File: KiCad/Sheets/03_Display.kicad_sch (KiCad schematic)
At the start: 1 part, among them U2 OLED_SSD1306_SPI_0.96

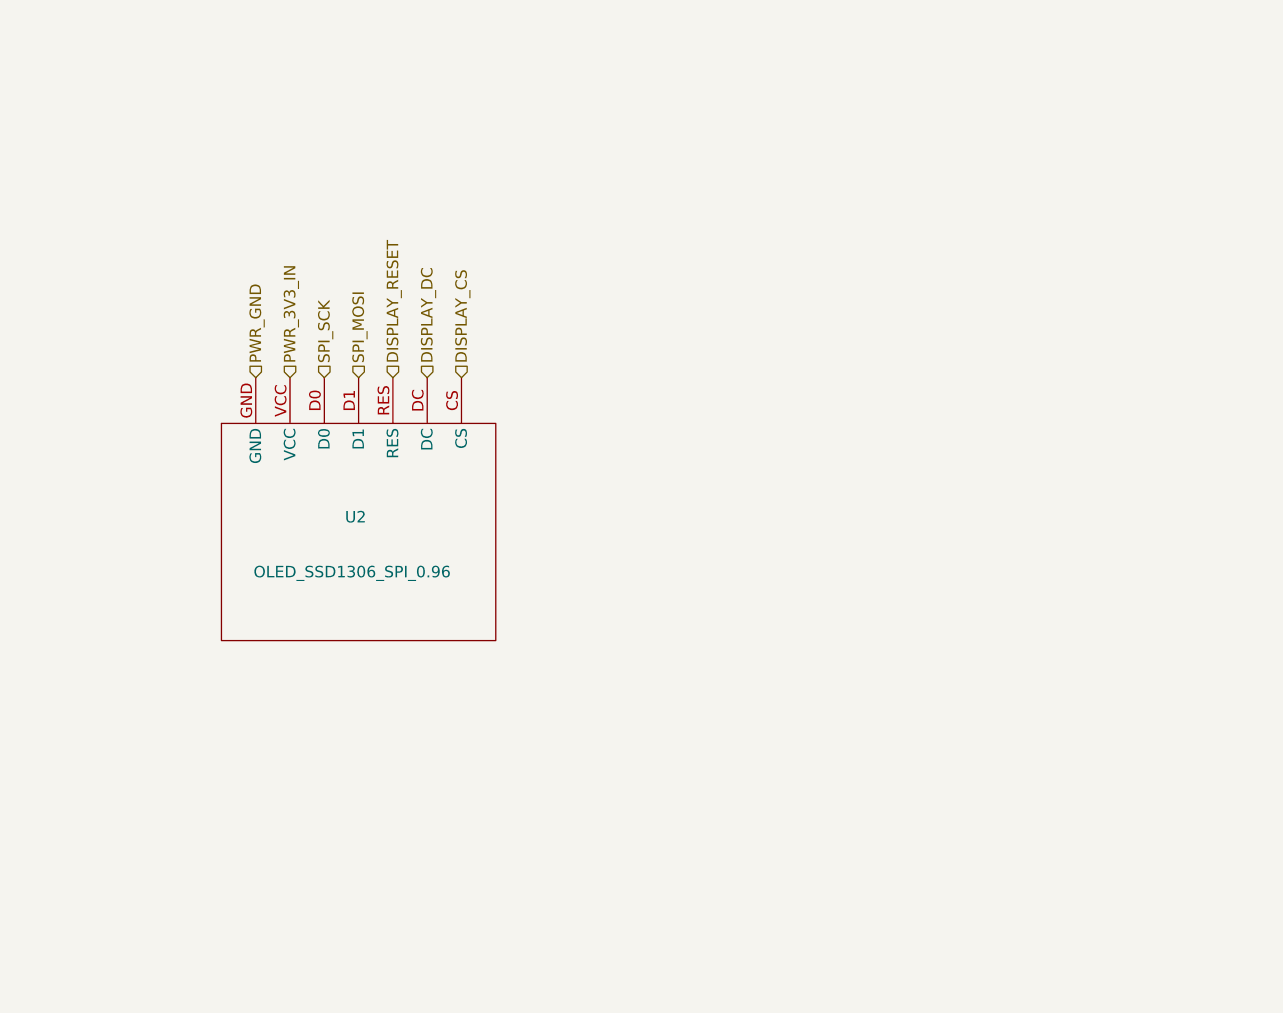
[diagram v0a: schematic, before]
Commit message: Footprints are created and assigned
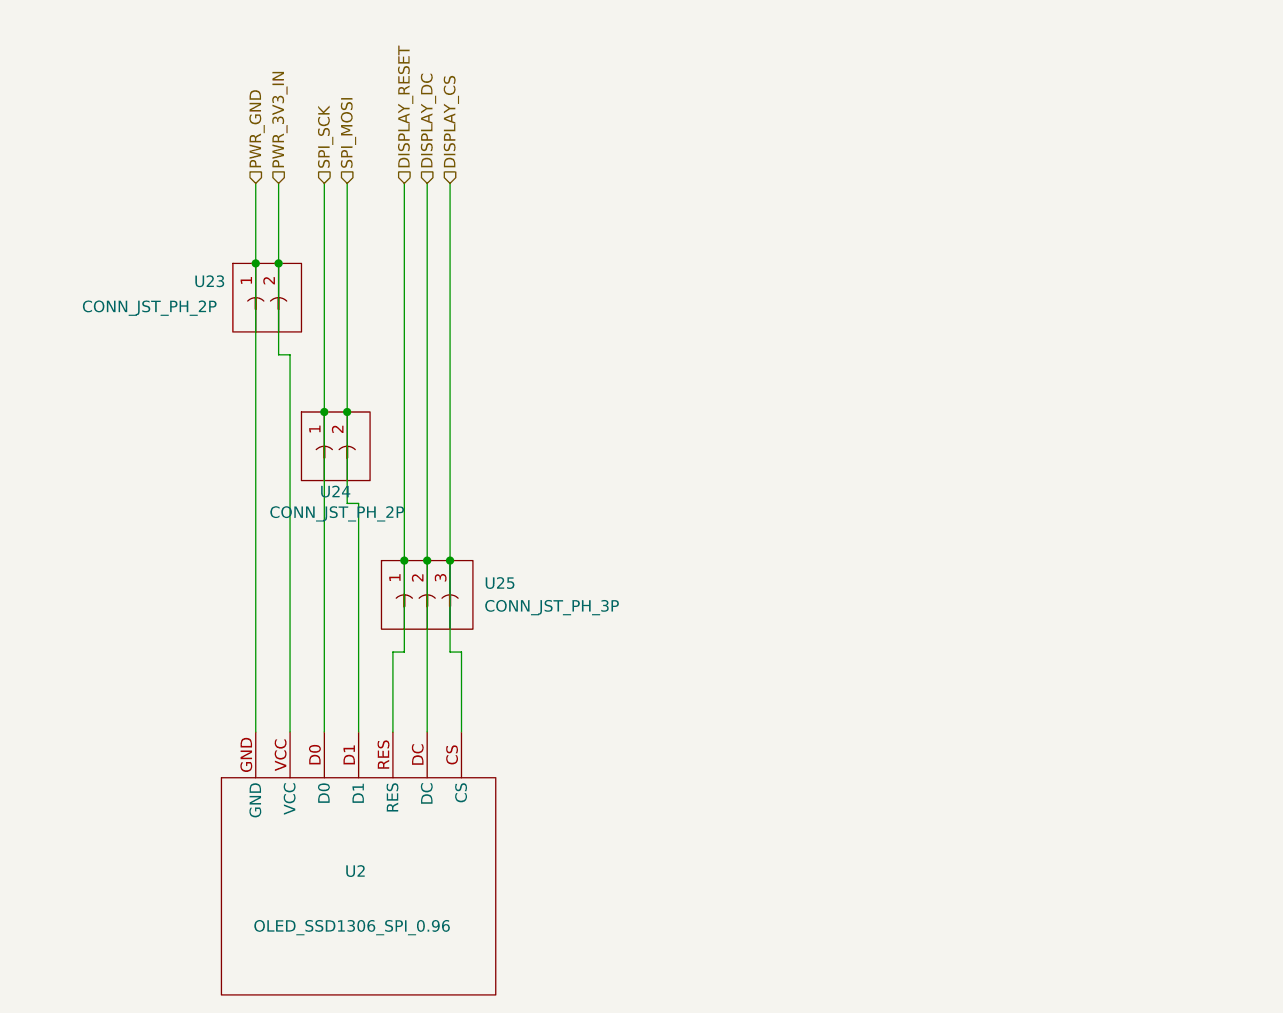
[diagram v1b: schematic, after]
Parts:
- added U23, U24: CONN_JST_PH_2P, Connector_JST:JST_PH_B2B-PH-K_1x02_P2.00mm_Vertical, symbol HMS_Symbols:CONN_JST_PH_2P
- added U25: CONN_JST_PH_3P, Connector_JST:JST_PH_B3B-PH-K_1x03_P2.00mm_Vertical, symbol HMS_Symbols:CONN_JST_PH_3P
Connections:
- net DISPLAY_CS: now also U25.3
- net DISPLAY_DC: now also U25.2
- net DISPLAY_RESET: now also U25.1
- net PWR_3V3_IN: now also U23.2
- net PWR_GND: now also U23.1
- net SPI_MOSI: now also U24.2
- net SPI_SCK: now also U24.1
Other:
- moved on the sheet: U2

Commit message: LEDs sheet added, schematic finished
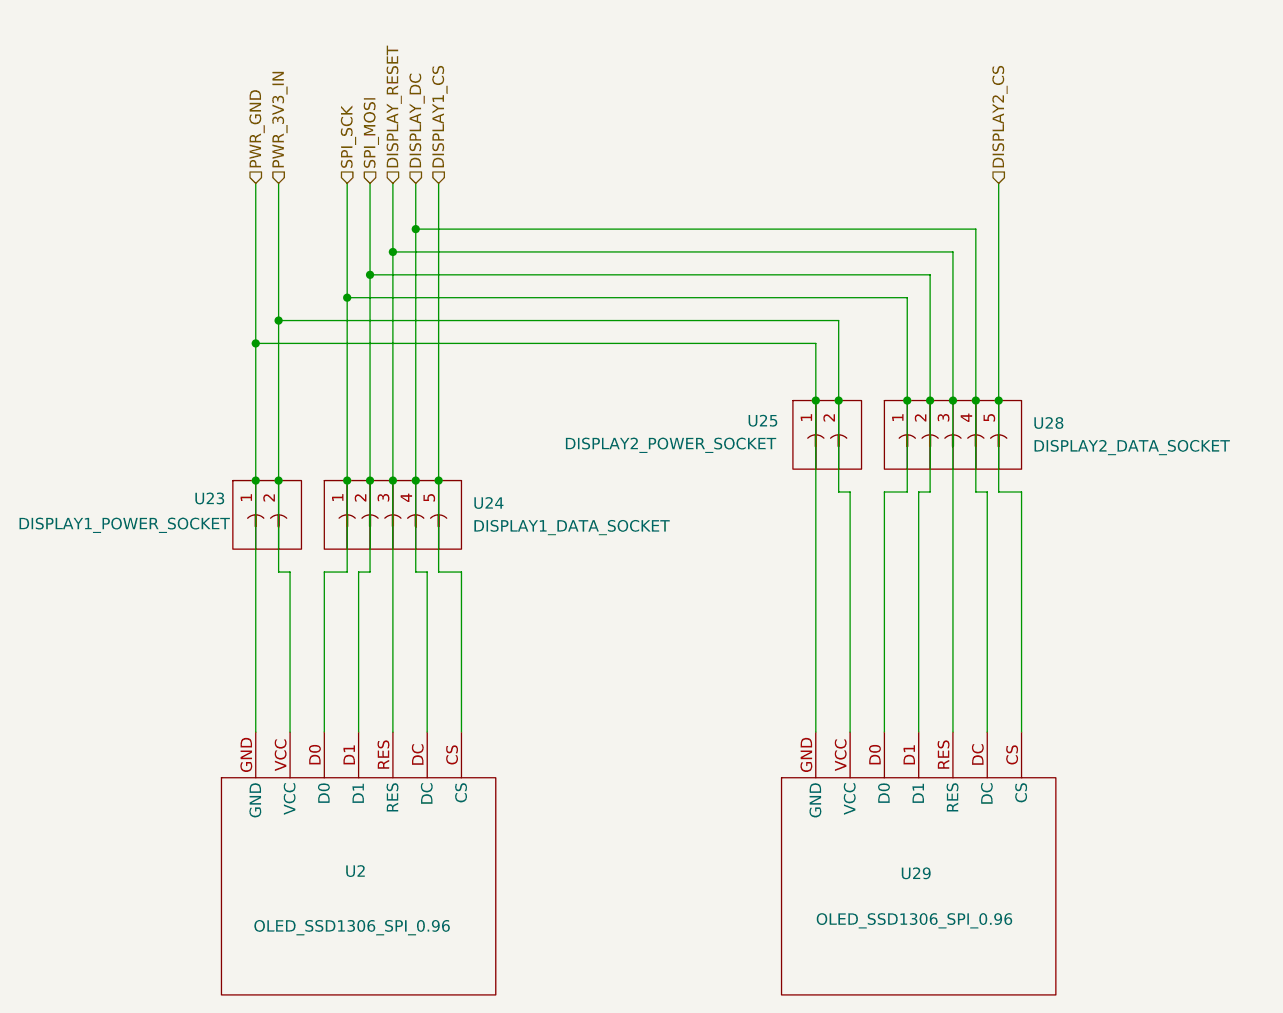
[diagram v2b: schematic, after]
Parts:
- removed U24: CONN_JST_PH_2P, Connector_JST:JST_PH_B2B-PH-K_1x02_P2.00mm_Vertical, symbol HMS_Symbols:CONN_JST_PH_2P
- removed U25: CONN_JST_PH_3P, Connector_JST:JST_PH_B3B-PH-K_1x03_P2.00mm_Vertical, symbol HMS_Symbols:CONN_JST_PH_3P
- added U24: DISPLAY1_DATA_SOCKET, Connector_JST:JST_PH_B5B-PH-K_1x05_P2.00mm_Vertical, symbol HMS_Symbols:CONN_JST_PH_5P
- added U25: DISPLAY2_POWER_SOCKET, Connector_JST:JST_PH_B2B-PH-K_1x02_P2.00mm_Vertical, symbol HMS_Symbols:CONN_JST_PH_2P
- added U28: DISPLAY2_DATA_SOCKET, Connector_JST:JST_PH_B5B-PH-K_1x05_P2.00mm_Vertical, symbol HMS_Symbols:CONN_JST_PH_5P
- added U29: OLED_SSD1306_SPI_0.96, symbol HMS_Symbols:OLED_SSD1306_SPI_0.96
- U23: value CONN_JST_PH_2P -> DISPLAY1_POWER_SOCKET
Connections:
- net DISPLAY_DC: now also U24.4, U28.4, U29.DC
- net DISPLAY_RESET: now also U24.3, U28.3, U29.RES
- net PWR_3V3_IN: now also U25.2, U29.VCC
- net PWR_GND: now also U25.1, U29.GND
- net SPI_MOSI: now also U24.2, U28.2, U29.D1
- net SPI_SCK: now also U24.1, U28.1, U29.D0
- net DISPLAY_CS renamed DISPLAY1_CS
- net DISPLAY1_CS: now also U24.5
- new net DISPLAY2_CS: U28.5, U29.CS
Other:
- moved on the sheet: U23

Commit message: Finished PCB
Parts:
- added R14, R15: 100Ω, Resistor_THT:R_Axial_DIN0207_L6.3mm_D2.5mm_P7.62mm_Horizontal, symbol Device:R
- U23, U25: footprint Connector_JST:JST_PH_B2B-PH-K_1x02_P2.00mm_Vertical -> Connector_JST:JST_XH_B2B-XH-A_1x02_P2.50mm_Vertical
- U24, U28: footprint Connector_JST:JST_PH_B5B-PH-K_1x05_P2.00mm_Vertical -> Connector_JST:JST_XH_B5B-XH-A_1x05_P2.50mm_Vertical
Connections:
- net DISPLAY1_CS: now also R14.1; no longer U2.CS, U24.5
- net DISPLAY2_CS: now also R15.1; no longer U28.5, U29.CS
- new net: R14.2, U2.CS, U24.5
- new net: R15.2, U28.5, U29.CS
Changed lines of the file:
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@@
 	(wire
 		(pts
-			(xy 214.63 63.5) (xy 214.63 87.63)
+			(xy 214.63 63.5) (xy 214.63 71.12)
 		)
 		(stroke
@@
 	(wire
 		(pts
-			(xy 152.4 63.5) (xy 152.4 96.52)
+			(xy 152.4 63.5) (xy 152.4 83.82)
 		)
 		(stroke
@@
 	(wire
 		(pts
+			(xy 152.4 91.44) (xy 152.4 96.52)
+		)
+		(stroke
+			(width 0.254)
+			(type default)
+			(color 255 153 0 1)
+		)
+	)
+	(wire
+		(pts
 			(xy 144.78 63.5) (xy 144.78 73.66)
 		)
@@
 			(type default)
 			(color 255 153 0 1)
+		)
+	)
+	(wire
+		(pts
+			(xy 214.63 78.74) (xy 214.63 87.63)
+		)
+		(stroke
+			(width 0.254)
+			(type default)
+			(color 132 132 132 1)
 		)
 	)
@@
 			)
 		)
-		(property "Footprint" "Connector_JST:JST_PH_B5B-PH-K_1x05_P2.00mm_Vertical"
+		(property "Footprint" "Connector_JST:JST_XH_B5B-XH-A_1x05_P2.50mm_Vertical"
 			(at 147.32 106.934 0)
 			(hide yes)
@@
 	)
 	(symbol
+		(lib_id "Device:R")
+		(at 214.63 74.93 0)
+		(unit 1)
+		(body_style 1)
+		(exclude_from_sim no)
+		(in_bom yes)
+		(on_board yes)
+		(in_pos_files yes)
+		(dnp no)
+		(fields_autoplaced yes)
+		(property "Reference" "R15"
+			(at 217.17 73.6599 0)
+			(show_name no)
+			(do_not_autoplace no)
+			(effects
+				(font
+					(size 1.27 1.27)
+				)
+				(justify left)
+			)
+		)
+		(property "Value" "100Ω"
+			(at 217.17 76.1999 0)
+			(show_name no)
+			(do_not_autoplace no)
+			(effects
+				(font
+					(size 1.27 1.27)
+				)
+				(justify left)
+			)
+		)
+		(property "Footprint" "Resistor_THT:R_Axial_DIN0207_L6.3mm_D2.5mm_P7.62mm_Horizontal"
+			(at 212.852 74.93 90)
+			(hide yes)
+			(show_name no)
+			(do_not_autoplace no)
+			(effects
+				(font
+					(size 1.27 1.27)
+				)
+			)
+		)
+		(property "Datasheet" ""
+			(at 214.63 74.93 0)
+			(hide yes)
+			(show_name no)
+			(do_not_autoplace no)
+			(effects
+				(font
+					(size 1.27 1.27)
+				)
+			)
+		)
+		(property "Description" "Resistor"
+			(at 214.63 74.93 0)
+			(hide yes)
+			(show_name no)
+			(do_not_autoplace no)
+			(effects
+				(font
+					(size 1.27 1.27)
+				)
+			)
+		)
+		(pin "2"
+		)
+		(pin "1"
+		)
+		(instances
+			(project "HMS_Master"
+				(path "/cab65a7d-0a7e-481c-9f85-25eca3c1fa1e/601e20f9-bdbc-41c4-99b3-024941b7a844"
+					(reference "R15")
+					(unit 1)
+				)
+			)
+		)
+	)
+	(symbol
 		(lib_id "HMS_Symbols:CONN_JST_PH_2P")
 		(at 195.58 91.44 0)
@@
 			)
 		)
-		(property "Footprint" "Connector_JST:JST_PH_B2B-PH-K_1x02_P2.00mm_Vertical"
+		(property "Footprint" "Connector_JST:JST_XH_B2B-XH-A_1x02_P2.50mm_Vertical"
 			(at 195.58 97.028 0)
 			(hide yes)
@@
 				(path "/cab65a7d-0a7e-481c-9f85-25eca3c1fa1e/601e20f9-bdbc-41c4-99b3-024941b7a844"
 					(reference "U25")
+					(unit 1)
+				)
+			)
+		)
+	)
+	(symbol
+		(lib_id "Device:R")
+		(at 152.4 87.63 0)
+		(unit 1)
+		(body_style 1)
+		(exclude_from_sim no)
+		(in_bom yes)
+		(on_board yes)
+		(in_pos_files yes)
+		(dnp no)
+		(fields_autoplaced yes)
+		(property "Reference" "R14"
+			(at 154.94 86.3599 0)
+			(show_name no)
+			(do_not_autoplace no)
+			(effects
+				(font
+					(size 1.27 1.27)
+				)
+				(justify left)
+			)
+		)
+		(property "Value" "100Ω"
+			(at 154.94 88.8999 0)
+			(show_name no)
+			(do_not_autoplace no)
+			(effects
+				(font
+					(size 1.27 1.27)
+				)
+				(justify left)
+			)
+		)
+		(property "Footprint" "Resistor_THT:R_Axial_DIN0207_L6.3mm_D2.5mm_P7.62mm_Horizontal"
+			(at 150.622 87.63 90)
+			(hide yes)
+			(show_name no)
+			(do_not_autoplace no)
+			(effects
+				(font
+					(size 1.27 1.27)
+				)
+			)
+		)
+		(property "Datasheet" ""
+			(at 152.4 87.63 0)
+			(hide yes)
+			(show_name no)
+			(do_not_autoplace no)
+			(effects
+				(font
+					(size 1.27 1.27)
+				)
+			)
+		)
+		(property "Description" "Resistor"
+			(at 152.4 87.63 0)
+			(hide yes)
+			(show_name no)
+			(do_not_autoplace no)
+			(effects
+				(font
+					(size 1.27 1.27)
+				)
+			)
+		)
+		(pin "2"
+		)
+		(pin "1"
+		)
+		(instances
+			(project "HMS_Master"
+				(path "/cab65a7d-0a7e-481c-9f85-25eca3c1fa1e/601e20f9-bdbc-41c4-99b3-024941b7a844"
+					(reference "R14")
 					(unit 1)
 				)
@@
 			)
 		)
-		(property "Footprint" "Connector_JST:JST_PH_B2B-PH-K_1x02_P2.00mm_Vertical"
+		(property "Footprint" "Connector_JST:JST_XH_B2B-XH-A_1x02_P2.50mm_Vertical"
 			(at 133.35 105.918 0)
 			(hide yes)
@@
 			)
 		)
-		(property "Footprint" "Connector_JST:JST_PH_B5B-PH-K_1x05_P2.00mm_Vertical"
+		(property "Footprint" "Connector_JST:JST_XH_B5B-XH-A_1x05_P2.50mm_Vertical"
 			(at 209.55 98.044 0)
 			(hide yes)
